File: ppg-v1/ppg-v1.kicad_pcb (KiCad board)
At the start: 2 copper layers, 56 parts, among them J1 USB_microB_2040002-1, J2 Conn_01x04_Male, SW1 SW_Push, SW2 SW_Push, SW3 PCM12, U1 STM32F411CEUx, U2 MCP73831T-2ACI/OT, U3 Opamp_Dual_Generic, U4 Opamp_Dual_Generic, U5 TPS2113APW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

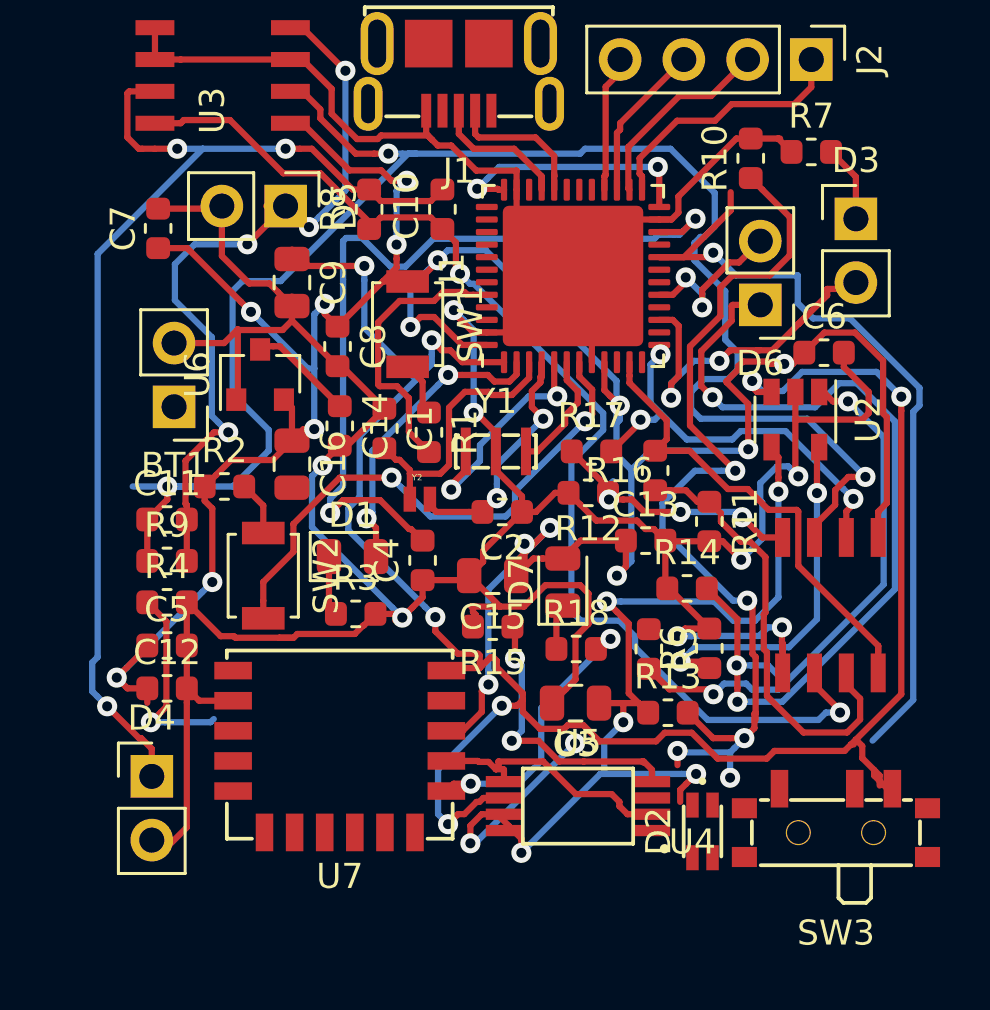
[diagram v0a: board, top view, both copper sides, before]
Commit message: Replace led footprint, move switch, route things
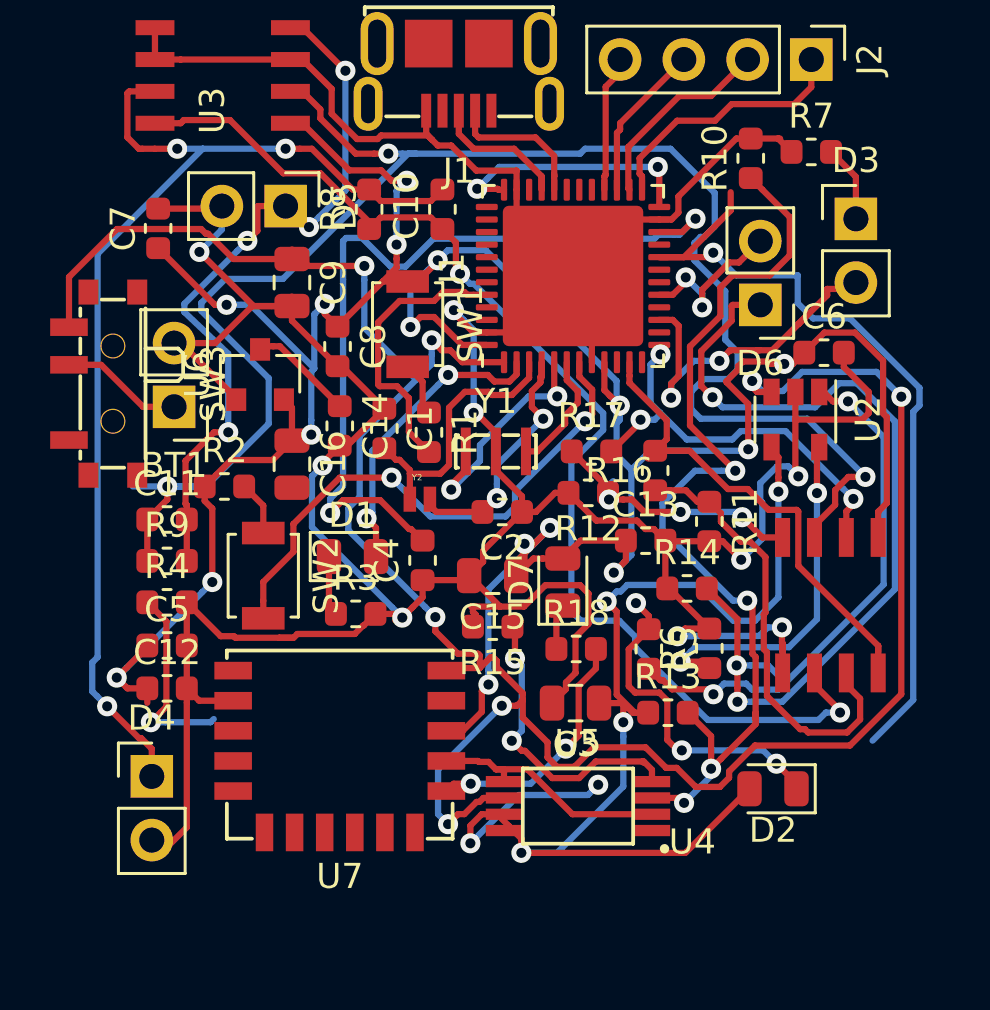
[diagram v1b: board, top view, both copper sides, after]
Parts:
- D2: value IN-S85TATRGB_ALT -> LED_Small; footprint rcpaperplane:IN-S85TATRGB -> LED_SMD:LED_0805_2012Metric
- moved SW3 33.9 mm to (138.2, 95.8), turned to 90 degrees
- moved D2 3.28 mm to (164.5, 112.0), turned to 180 degrees
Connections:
- D2 pad 2: (no net) -> Net-(C3-Pad1)
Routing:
- net Net-(D2-Pad1): track 0.00 -> 13.3 mm, vias 0 -> 3
- net VBAT: track 83.6 -> 94.1 mm
- net Net-(C3-Pad1): track 35.4 -> 41.5 mm, vias 5 -> 4
- net Net-(BT1-Pad1): track 0.00 -> 4.88 mm
- net GND: track 178.6 -> 180.2 mm, vias 8 -> 9
- net Net-(R18-Pad2): track 11.0 -> 9.93 mm
- net Net-(C11-Pad2): track 31.2 -> 30.4 mm
- net Net-(C11-Pad1): track 69.2 -> 70.0 mm
- net Net-(R15-Pad1): track 11.5 -> 12.0 mm
- net Net-(R10-Pad1): track 38.0 -> 38.3 mm, vias 5 -> 4

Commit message: Rebuilding pcb layout
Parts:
- moved R9 88.2 mm to (224.3, 75.9), turned to 90 degrees
- moved C11 86.3 mm to (222.8, 75.9), turned to 90 degrees
- moved R17 81.7 mm to (235.2, 74.3), turned to 270 degrees
- moved BT1 81.1 mm to (212.3, 58.9), turned to 270 degrees
- moved R12 80.8 mm to (233.4, 73.7), turned to 90 degrees
- moved SW3 80.2 mm to (211.6, 63.7), turned to 0 degrees
- moved C12 78.8 mm to (212.7, 76.9), turned to 270 degrees
- moved C13 78.3 mm to (233.6, 77.1), turned to 270 degrees
- moved D5 77.4 mm to (220.7, 72.5), turned to 90 degrees
- moved D4 71.5 mm to (199.6, 72.5), turned to 90 degrees
- moved U5 69.4 mm to (193.2, 53.6), turned to 0 degrees
- moved C14 67.7 mm to (202.9, 59.1), turned to 90 degrees
- moved R13 67.7 mm to (195.5, 51.2), turned to 180 degrees
- moved U6 67.2 mm to (200.4, 58.9), turned to 270 degrees
- moved C15 66.7 mm to (200.3, 56.3), turned to 0 degrees
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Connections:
- C16 pad 2: Net-(C16-Pad2) -> GND
- U1 pad 25: Net-(J2-Pad1) -> /CTS
- U1 pad 26: Net-(J2-Pad2) -> /RST_N
- U1 pad 27: Net-(J2-Pad3) -> /RTS
- U1 pad 28: Net-(J2-Pad4) -> /TX
- U1 pad 29: Net-(U1-Pad29) -> /RX
- U1 pad 30: Net-(U1-Pad30) -> /RX_IND
- U1 pad 37: Net-(U1-Pad37) -> Net-(J2-Pad1)
- U1 pad 39: Net-(U1-Pad39) -> Net-(J2-Pad2)
- U1 pad 41: Net-(U1-Pad41) -> Net-(J2-Pad3)
- U1 pad 43: Net-(U1-Pad43) -> Net-(J2-Pad4)
- U3 pad 5: GND -> Net-(C10-Pad1)
- U3 pad 6: Net-(C11-Pad2) -> Net-(R11-Pad1)
- U3 pad 7: Net-(C11-Pad1) -> PhotoDiode1
- U4 pad 1: PhotoDiode1 -> Net-(C11-Pad1)
- U4 pad 2: Net-(R11-Pad1) -> Net-(C11-Pad2)
- U4 pad 3: Net-(C10-Pad1) -> GND
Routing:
- net +3V3: track 131.1 -> 13.7 mm, vias 18 -> 0
- net GND: track 180.2 -> 79.9 mm, vias 9 -> 0
- net VBAT: track 94.1 -> 17.4 mm, vias 7 -> 0
- net Net-(C11-Pad1): track 70.0 -> 9.89 mm, vias 3 -> 0
- net Net-(C10-Pad2): track 44.6 -> 7.17 mm, vias 3 -> 0
- net Net-(C10-Pad1): track 47.2 -> 10.1 mm, vias 2 -> 0
- net Net-(C3-Pad1): track 41.5 -> 8.26 mm, vias 4 -> 0
- net Net-(D6-Pad1): track 35.7 -> 3.11 mm, vias 3 -> 0
- net Net-(R10-Pad1): track 38.3 -> 6.06 mm, vias 4 -> 0
- net Net-(R4-Pad1): track 40.4 -> 9.33 mm
- net Net-(C4-Pad2): track 32.6 -> 6.27 mm
- net Net-(C11-Pad2): track 30.4 -> 7.43 mm, vias 4 -> 0
- net Net-(R5-Pad2): track 20.9 -> 1.74 mm, vias 2 -> 0
- net Net-(R11-Pad1): track 17.9 -> 4.52 mm
- net Net-(R6-Pad1): track 14.2 -> 1.67 mm, vias 2 -> 0
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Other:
- net class Default: trace_width 0.25 -> 0.2; via_dia 0.8 -> 0.6096; via_drill 0.4 -> 0.3047

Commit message: Draft 1 of the PCBgit add .
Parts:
- moved D5 54.0 mm to (186.1, 113.9), turned to 270 degrees
- moved R12 52.4 mm to (199.2, 113.3)
- moved R17 52.2 mm to (200.7, 113.5)
- moved U4 52.2 mm to (191.9, 116.2)
- moved C11 52.0 mm to (188.7, 115.1)
- moved R9 52.0 mm to (190.2, 115.1)
- moved C13 51.5 mm to (199.9, 116.1), turned to 0 degrees
- moved R8 48.6 mm to (173.9, 114.7), turned to 180 degrees
- moved R11 48.5 mm to (180.8, 110.2)
- moved U3 48.5 mm to (173.5, 113.2)
- moved C12 48.5 mm to (180.8, 113.5)
- moved R16 47.7 mm to (182.4, 110.3), turned to 90 degrees
- moved SW3 47.6 mm to (174.4, 93.5), turned to 270 degrees
- moved C10 45.8 mm to (177.2, 114.7), turned to 0 degrees
- moved BT1 44.9 mm to (177.4, 87.2), turned to 90 degrees
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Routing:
- net GND: track 79.9 -> 189.0 mm, vias 0 -> 10
- net +3V3: track 13.7 -> 103.1 mm, vias 0 -> 13
- net PhotoDiode2: track 9.19 -> 31.1 mm, vias 0 -> 4
- net Net-(C3-Pad1): track 8.26 -> 27.9 mm
- net Net-(C14-Pad1): track 2.58 -> 20.0 mm, vias 0 -> 2
- net Net-(R10-Pad1): track 6.06 -> 21.4 mm, vias 0 -> 2
- net VBAT: track 17.4 -> 31.8 mm
- net USBD+: track 0.00 -> 12.2 mm
- net USBD-: track 0.00 -> 11.9 mm
- net Net-(R1-Pad2): track 0.00 -> 10.4 mm
- net Net-(C10-Pad2): track 7.17 -> 16.4 mm
- net /CTS: track 0.00 -> 6.57 mm
- net /RST_N: track 0.00 -> 5.97 mm
- net Net-(J2-Pad4): track 0.00 -> 5.83 mm
- net /RTS: track 0.00 -> 5.65 mm
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- added copper zone on F.Cu, net (none)
- added copper zone on B.Cu, net GND
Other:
- board outline added: 30.5 x 36.1 mm

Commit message: fix buttons
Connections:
- R1 pad 2: Net-(R1-Pad2) -> GND
- SW2 pad 2: Net-(SW2-Pad2) -> GND
- U1 pad 44: Net-(R1-Pad2) -> Net-(R1-Pad1)
- U1 pad 7: Net-(SW2-Pad2) -> Net-(R2-Pad2)
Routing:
- net GND: track 189.0 -> 205.3 mm, vias 10 -> 12
- net Net-(R2-Pad2): track 5.80 -> 17.3 mm
- net Net-(R1-Pad2): track 10.4 -> 0.00 mm
- net Net-(SW2-Pad2): track 9.87 -> 0.00 mm
- net Net-(R1-Pad1): track 3.14 -> 12.9 mm
- net USBD+: track 12.2 -> 10.4 mm
- net USBD-: track 11.9 -> 10.3 mm
